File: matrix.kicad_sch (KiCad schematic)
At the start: 134 parts, among them SW1 SW_Push, SW10 SW_Push, SW11 SW_Push, SW12 SW_Push, SW13 SW_Push, SW14 SW_Push, SW15 SW_Push, SW16 SW_Push, SW17 SW_Push, SW18 SW_Push, SW19 SW_Push, SW2 SW_Push, SW20 SW_Push, SW21 SW_Push, SW22 SW_Push, SW23 SW_Push, SW24 SW_Push, SW25 SW_Push, SW26 SW_Push, SW27 SW_Push, SW28 SW_Push, SW29 SW_Push, SW3 SW_Push, SW30 SW_Push, SW31 SW_Push, SW32 SW_Push, SW33 SW_Push, SW34 SW_Push, SW35 SW_Push, SW36 SW_Push, SW37 SW_Push, SW38 SW_Push, SW39 SW_Push, SW4 SW_Push, SW40 SW_Push, SW41 SW_Push, SW42 SW_Push, SW43 SW_Push, SW44 SW_Push, SW45 SW_Push, SW46 SW_Push, SW47 SW_Push, SW48 SW_Push, SW49 SW_Push, SW5 SW_Push, SW50 SW_Push, SW51 SW_Push, SW52 SW_Push, SW53 SW_Push, SW54 SW_Push, SW55 SW_Push, SW56 SW_Push, SW57 SW_Push, SW58 SW_Push, SW59 SW_Push, SW6 SW_Push, SW60 SW_Push, SW61 SW_Push, SW62 SW_Push, SW63 SW_Push, SW64 SW_Push, SW65 SW_Push, SW66 SW_Push, SW67 SW_Push, SW7 SW_Push, SW8 SW_Push, SW9 SW_Push

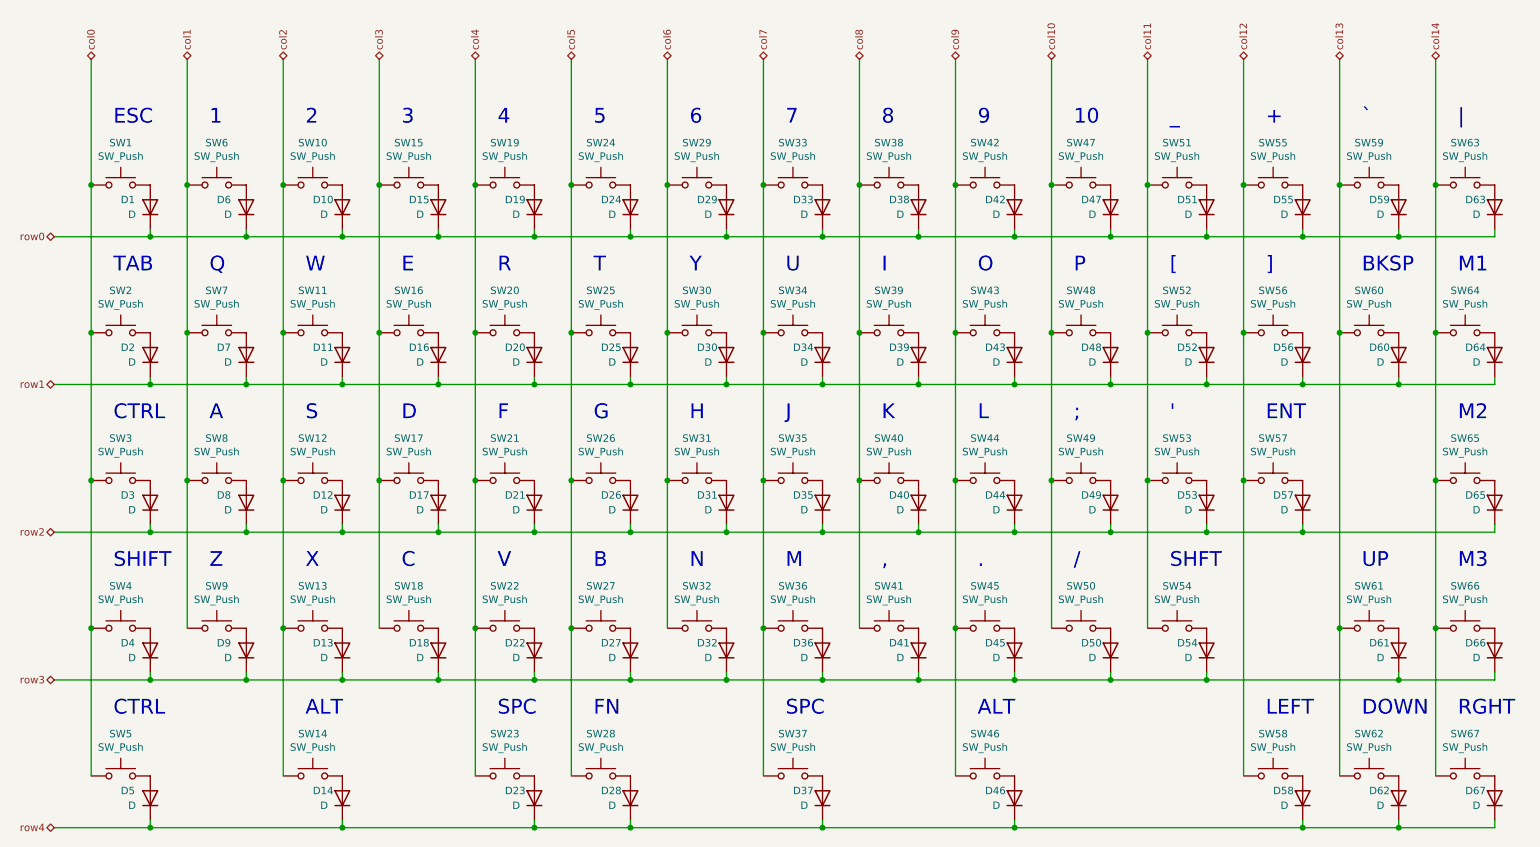
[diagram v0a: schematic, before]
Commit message: Change USB port, add DB conn, add some keys
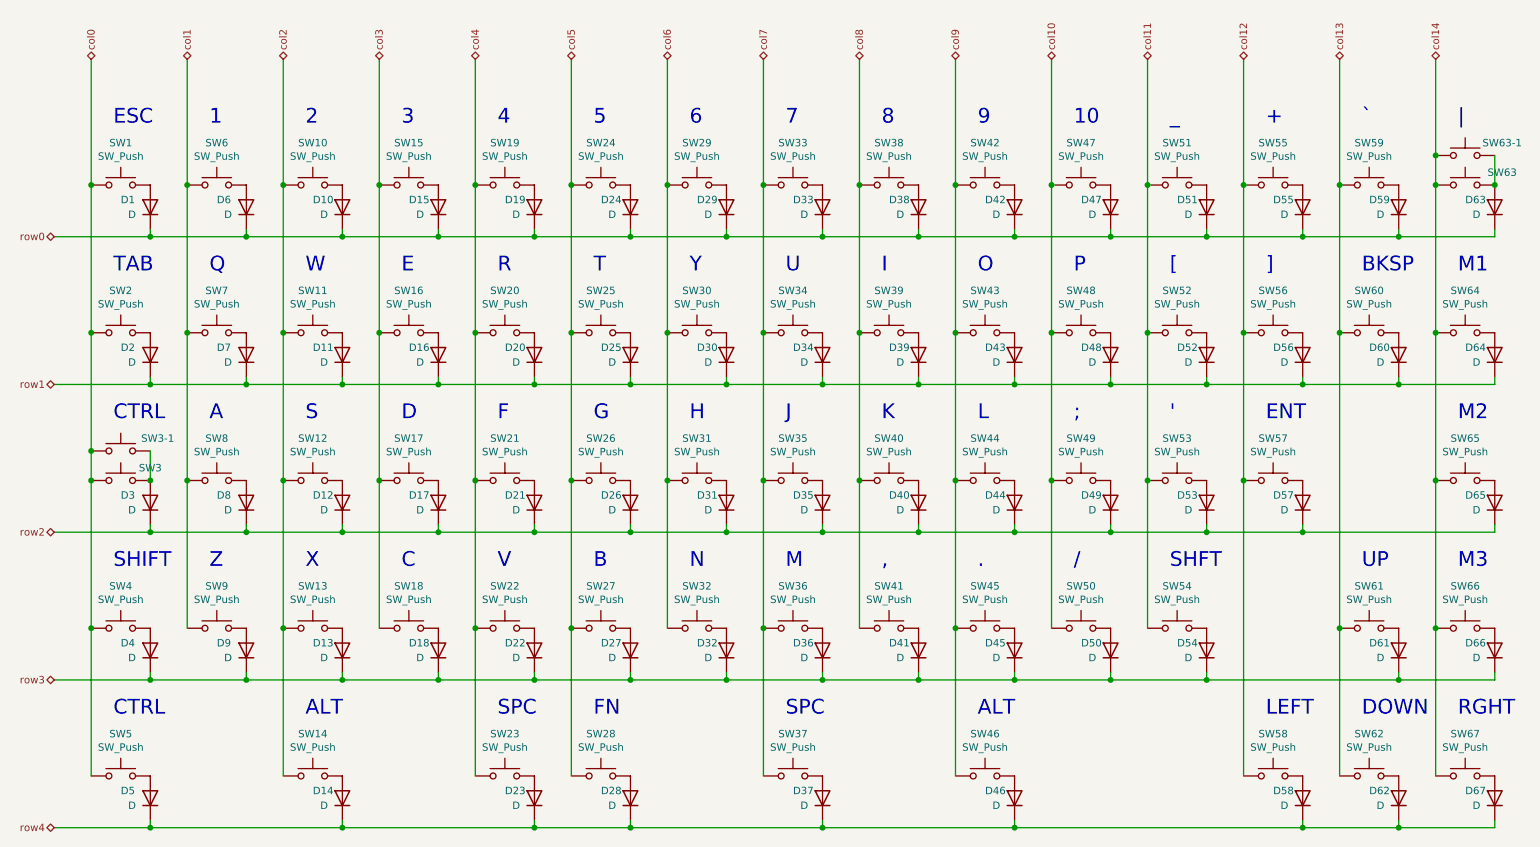
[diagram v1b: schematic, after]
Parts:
- added SW3-1: SW_Push, footprints:CHERRY_PLATE_125H, symbol Switch:SW_Push
- added SW63-1: SW_Push, footprints:CHERRY_PCB_200H, symbol Switch:SW_Push
- D1, D10, D11, D12, D13, D14, D15, D16, D17, D18, D19, D2, D20, D21, D22, D23, D24, D25, D26, D27, D28, D29, D3, D30, D31, D32, D33, D34, D35, D36, D37, D38, D39, D4, D40, D41, D42, D43, D44, D45, D46, D47, D48, D49, D5, D50, D51, D52, D53, D54, D55, D56, D57, D58, D59, D6, D60, D61, D62, D63, D64, D65, D66, D67, D7, D8, D9: footprint Diodes_SMD:D_SOD-123 -> footprints:D_SOD-123
- SW1, SW10, SW11, SW12, SW13, SW15, SW16, SW17, SW18, SW19, SW20, SW21, SW22, SW24, SW25, SW26, SW27, SW28, SW29, SW30, SW31, SW32, SW33, SW34, SW35, SW36, SW38, SW39, SW40, SW41, SW42, SW43, SW44, SW45, SW47, SW48, SW49, SW50, SW51, SW52, SW53, SW55, SW56, SW58, SW59, SW6, SW61, SW62, SW63, SW64, SW65, SW66, SW67, SW7, SW8, SW9: footprint MX_Switch:SW_Cherry_MX_1.00u_PCB -> footprints:CHERRY_PLATE_100H
- SW14, SW2, SW46, SW5, SW60: footprint MX_Switch:SW_Cherry_MX_1.50u_PCB -> footprints:CHERRY_PLATE_150H
- SW23: footprint MX_Switch:SW_Cherry_MX_2.00u_PCB_ReversedStabilizers -> footprints:CHERRY_PCB_200H_F
- SW3, SW54: footprint MX_Switch:SW_Cherry_MX_1.75u_PCB -> footprints:CHERRY_PLATE_175H
- SW37: footprint MX_Switch:SW_Cherry_MX_2.75u_PCB_ReversedStabilizers -> footprints:CHERRY_PCB_275H_F
- SW4: footprint MX_Switch:SW_Cherry_MX_2.25u_PCB -> footprints:CHERRY_PCB_225H
- SW57: footprint MX_Switch:SW_Cherry_MX_2.25u_PCB_ReversedStabilizers -> footprints:CHERRY_PCB_225H_F
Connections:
- net col0: now also SW3-1.1
- net col14: now also SW63-1.1
- net at D3.2 (A), SW3.2: now also SW3-1.2
- net at D63.2 (A), SW63.2: now also SW63-1.2
